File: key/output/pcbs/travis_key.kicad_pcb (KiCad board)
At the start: 2 copper layers, 38.1 x 38.1 mm, 4 parts

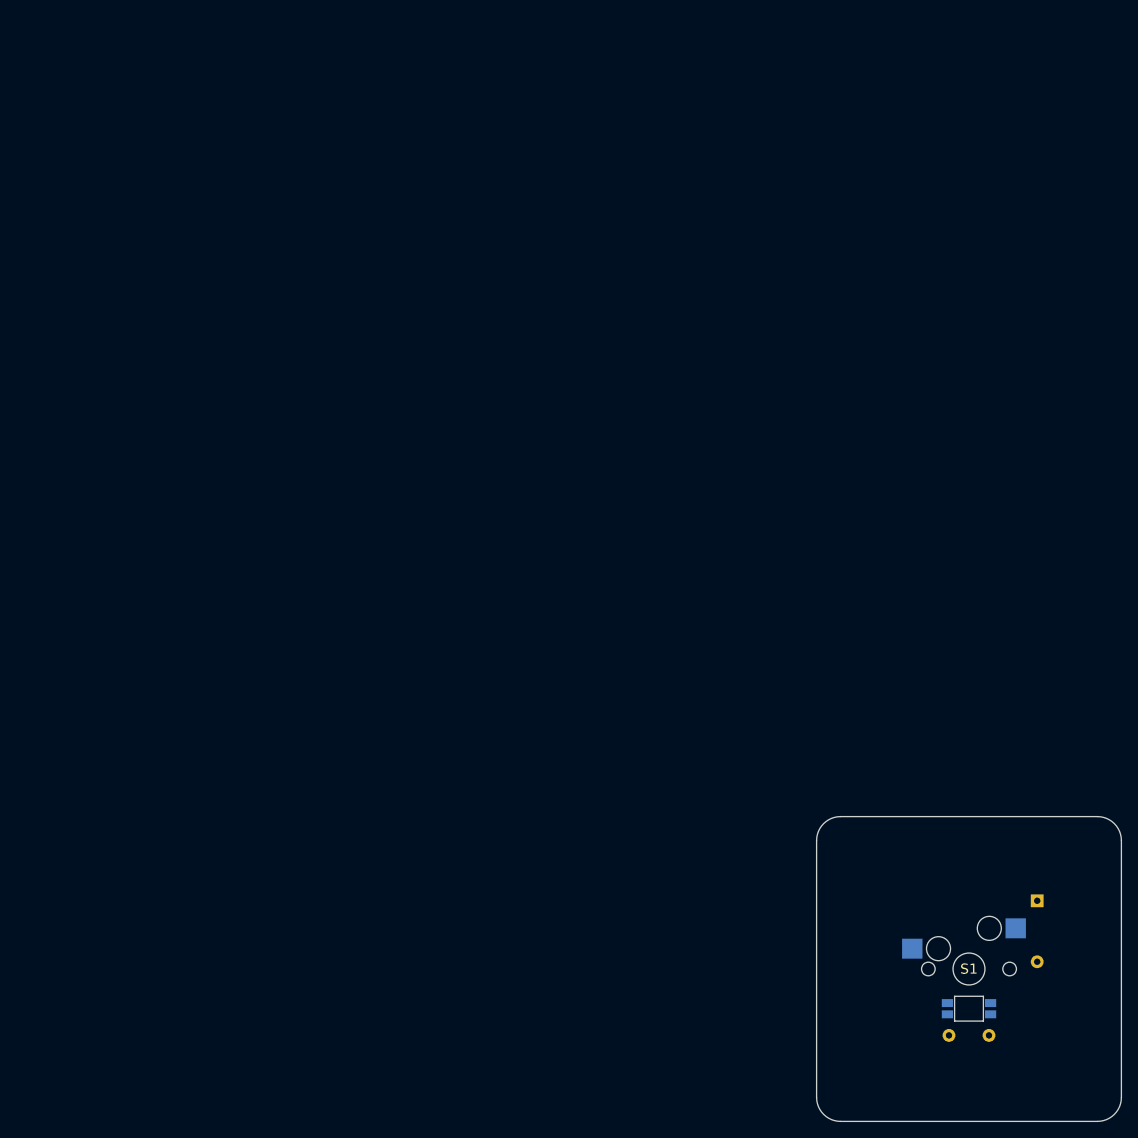
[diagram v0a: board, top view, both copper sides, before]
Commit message: key module functions with traces
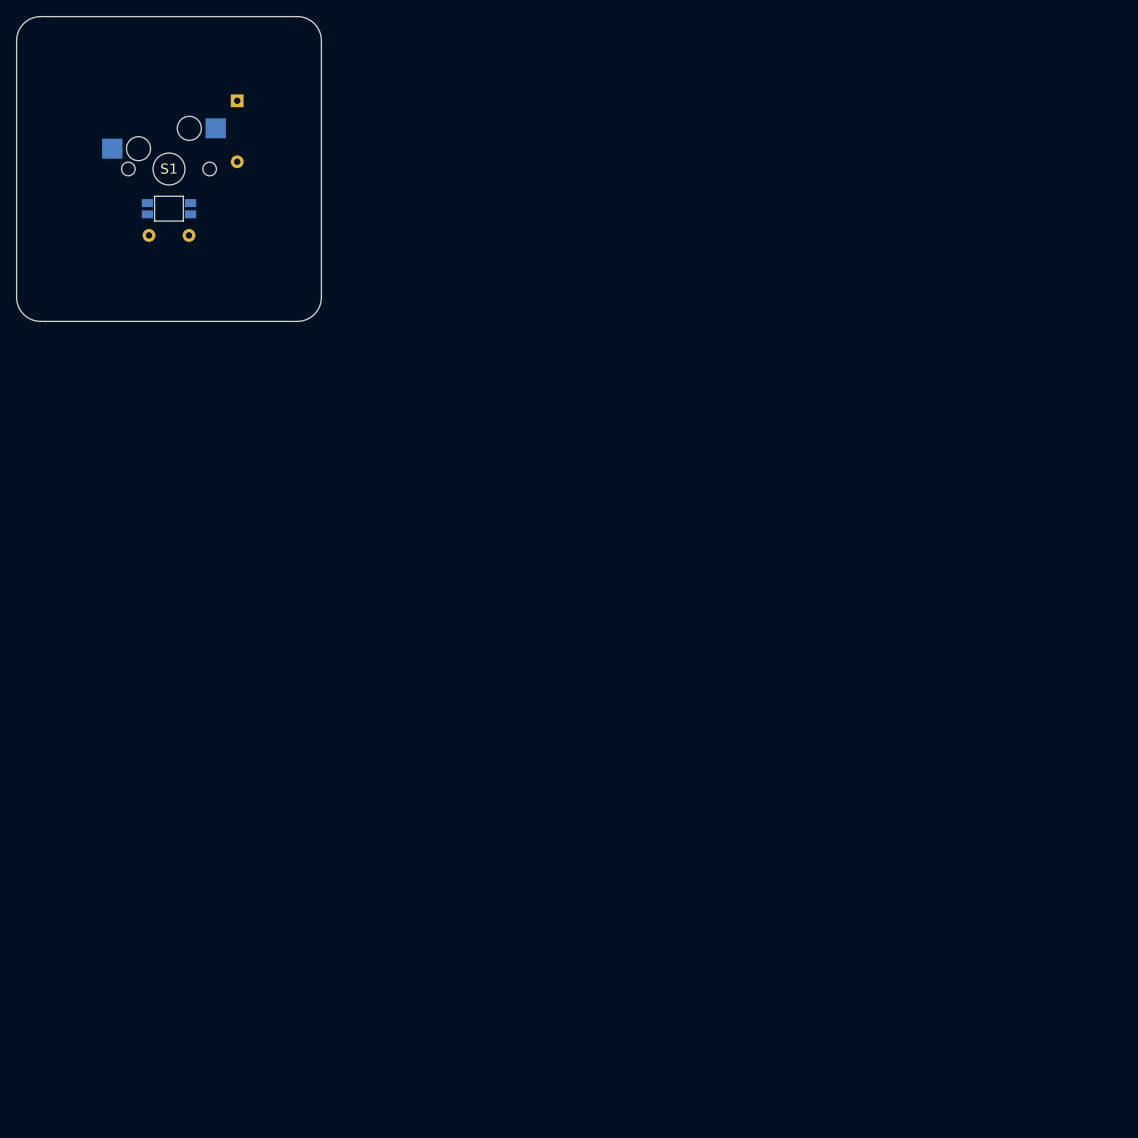
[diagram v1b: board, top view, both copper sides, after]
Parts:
- moved C1 141.4 mm to (2.50, 8.30)
- moved D1 141.4 mm to (8.53, -8.53)
- moved LED1 141.4 mm to (0.00, 4.96)
- moved S1 141.4 mm to (0.00, 0.00)
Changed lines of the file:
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@@
   )
       (module MX (layer F.Cu)
-      (at 100 100 0)
+      (at 0 0 0)
       (fp_text reference "S1" (at 0 0) (layer F.SilkS)  (effects (font (size 1.27 1.27) (thickness 0.15))))
       (fp_text value "" (at 0 0) (layer F.SilkS) hide (effects (font (size 1.27 1.27) (thickness 0.15))))
@@
     (descr "Diode, DO-35_SOD27 series, Axial, Horizontal, pin pitch=7.62mm, , length*diameter=4*2mm^2, , http://www.diodes.com/_files/packages/DO-35.pdf")
     (tags "Diode DO-35_SOD27 series Axial Horizontal pin pitch 7.62mm  length 4mm diameter 2mm")
-    (at 108.525 91.475 270)
+    (at 8.525 -8.525 270)
     (fp_text reference "D1" (at 3.81 -2.12 270) (layer "B.SilkS")
       (effects (font (size 1 1) (thickness 0.15)) (justify mirror))
@@
       (module "ceoloide:led_SK6812mini-e (per-keysingle-side)"
         (layer B.Cu)
-        (at 100 104.96 0)
+        (at 0 4.96 0)
         (fp_text reference "LED1" (at -4.75 0 90) (layer B.SilkS)
           (effects (font (size 1 1) (thickness 0.15)))
@@
         (polygon
           (pts
-            (xy 98.000 103.110)
-            (xy 102.000 103.110)
-            (xy 102.000 106.810)
-            (xy 98.000 106.810)
+            (xy -2.000 3.110)
+            (xy 2.000 3.110)
+            (xy 2.000 6.810)
+            (xy -2.000 6.810)
           )
         )
@@
     (descr "C, Disc series, Radial, pin pitch=5.00mm, , diameter*width=4.7*2.5mm^2, Capacitor, http://www.vishay.com/docs/45233/krseries.pdf")
     (tags "C Disc series Radial pin pitch 5.00mm  diameter 4.7mm width 2.5mm Capacitor")
-    (at 102.5 108.3 180)
+    (at 2.5 8.3 180)
     (fp_text reference "C1" (at 2.5 -2.5 180) (layer B.SilkS)
       (effects (font (size 1 1) (thickness 0.15)) (justify mirror))
     )
     (fp_text value "104" (at 2.5 2.5 180) (layer B.Fab)
-      (effects (font (size 1 1) (thickness 0.15)) (justify mirror))
+      (effects (font (size 1 1) (thickness 0.15)))
     )
     (fp_line (start 0.15 -1.25) (end 0.15 1.25) (layer B.Fab) (width 0.1))
@@
     )
   )
-            (gr_line (start 80.95 116.05) (end 80.95 83.95) (angle 90) (layer Edge.Cuts) (width 0.15))
-(gr_line (start 83.95 80.95) (end 116.05 80.95) (angle 90) (layer Edge.Cuts) (width 0.15))
-(gr_line (start 119.05 83.95) (end 119.05 116.05) (angle 90) (layer Edge.Cuts) (width 0.15))
-(gr_line (start 116.05 119.05) (end 83.95 119.05) (angle 90) (layer Edge.Cuts) (width 0.15))
-(gr_arc (start 83.95 83.95) (end 83.95 80.95) (angle -90) (layer Edge.Cuts) (width 0.15))
-(gr_arc (start 116.05 83.95) (end 119.05 83.95) (angle -90) (layer Edge.Cuts) (width 0.15))
-(gr_arc (start 116.05 116.05) (end 116.05 119.05) (angle -90) (layer Edge.Cuts) (width 0.15))
-(gr_arc (start 83.95 116.05) (end 80.95 116.05) (angle -90) (layer Edge.Cuts) (width 0.15))
+            (gr_line (start -19.05 16.05) (end -19.05 -16.05) (angle 90) (layer Edge.Cuts) (width 0.15))
+(gr_line (start -16.05 -19.05) (end 16.05 -19.05) (angle 90) (layer Edge.Cuts) (width 0.15))
+(gr_line (start 19.05 -16.05) (end 19.05 16.05) (angle 90) (layer Edge.Cuts) (width 0.15))
+(gr_line (start 16.05 19.05) (end -16.05 19.05) (angle 90) (layer Edge.Cuts) (width 0.15))
+(gr_arc (start -16.05 -16.05) (end -16.05 -19.05) (angle -90) (layer Edge.Cuts) (width 0.15))
+(gr_arc (start 16.05 -16.05) (end 19.05 -16.05) (angle -90) (layer Edge.Cuts) (width 0.15))
+(gr_arc (start 16.05 16.05) (end 16.05 19.05) (angle -90) (layer Edge.Cuts) (width 0.15))
+(gr_arc (start -16.05 16.05) (end -19.05 16.05) (angle -90) (layer Edge.Cuts) (width 0.15))
 )

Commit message: footprint wip
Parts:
- LED1: value (none) -> SK6812mini-e; footprint ceoloide:led_SK6812mini-e (per-keysingle-side) -> ceoloide:led_SK6812mini-e (per-key single-side)
- S1: value (none) -> Kailh MX Switch Sockets
- moved D1 0.50 mm to (8.53, -8.03)
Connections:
- net LED_0 renamed LED_2
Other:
- board text added: "C1"
- board text added: "D1"
- board text added: "LED_1"
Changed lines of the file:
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@@
   (title_block
     (title travis_key)
-    (rev 2024.03.20)
+    (rev 2024.03.23)
     (company "Travis Hardiman")
   )
@@
 (net 3 "row0")
 (net 4 "RAW")
-(net 5 "LED_0")
+(net 5 "LED_2")
 (net 6 "GND")
 (net 7 "LED_1")
@@
 (add_net "row0")
 (add_net "RAW")
-(add_net "LED_0")
+(add_net "LED_2")
 (add_net "GND")
 (add_net "LED_1")
   )
-      (module MX (layer F.Cu)
-      (at 0 0 0)
-      (fp_text reference "S1" (at 0 0) (layer F.SilkS)  (effects (font (size 1.27 1.27) (thickness 0.15))))
-      (fp_text value "" (at 0 0) (layer F.SilkS) hide (effects (font (size 1.27 1.27) (thickness 0.15))))
-      (fp_line (start -7 -6) (end -7 -7) (layer Dwgs.User) (width 0.15))
-      (fp_line (start -7 7) (end -6 7) (layer Dwgs.User) (width 0.15))
-      (fp_line (start -6 -7) (end -7 -7) (layer Dwgs.User) (width 0.15))
-      (fp_line (start -7 7) (end -7 6) (layer Dwgs.User) (width 0.15))
-      (fp_line (start 7 6) (end 7 7) (layer Dwgs.User) (width 0.15))
-      (fp_line (start 7 -7) (end 6 -7) (layer Dwgs.User) (width 0.15))
-      (fp_line (start 6 7) (end 7 7) (layer Dwgs.User) (width 0.15))
-      (fp_line (start 7 -7) (end 7 -6) (layer Dwgs.User) (width 0.15))
-      (pad "" np_thru_hole circle (at 0 0) (size 3.9878 3.9878) (drill 3.9878) (layers *.Cu *.Mask))
-      (pad "" np_thru_hole circle (at 5.08 0) (size 1.7018 1.7018) (drill 1.7018) (layers *.Cu *.Mask))
-      (pad "" np_thru_hole circle (at -5.08 0) (size 1.7018 1.7018) (drill 1.7018) (layers *.Cu *.Mask))
-      (fp_line (start -9.5 -9.5) (end 9.5 -9.5) (layer Dwgs.User) (width 0.15))
-      (fp_line (start 9.5 -9.5) (end 9.5 9.5) (layer Dwgs.User) (width 0.15))
-      (fp_line (start 9.5 9.5) (end -9.5 9.5) (layer Dwgs.User) (width 0.15))
-      (fp_line (start -9.5 9.5) (end -9.5 -9.5) (layer Dwgs.User) (width 0.15))
-        (pad "" np_thru_hole circle (at 2.54 -5.08) (size 3 3) (drill 3) (layers *.Cu *.Mask))
-        (pad "" np_thru_hole circle (at -3.81 -2.54) (size 3 3) (drill 3) (layers *.Cu *.Mask))
-        (pad 1 smd rect (at -7.085 -2.54 0) (size 2.55 2.5) (layers B.Cu B.Paste B.Mask) (net 1 "col0"))
-        (pad 2 smd rect (at 5.842 -5.08 0) (size 2.55 2.5) (layers B.Cu B.Paste B.Mask) (net 2 "single_A_one"))
-        )
+        (module MX (layer F.Cu)
+        (at 0 0 0)
+        (fp_text reference "S1" (at 0 -3.25) (layer F.SilkS)  (effects (font (size 1 1) (thickness 0.15))))
+        (fp_text value "Kailh MX Switch Sockets" (at 0 0) (layer B.Fab) hide (effects (font (size 1 1) (thickness 0.15))))
+        (fp_line (start -7 -6) (end -7 -7) (layer Dwgs.User) (width 0.15))
+        (fp_line (start -7 7) (end -6 7) (layer Dwgs.User) (width 0.15))
+        (fp_line (start -6 -7) (end -7 -7) (layer Dwgs.User) (width 0.15))
+        (fp_line (start -7 7) (end -7 6) (layer Dwgs.User) (width 0.15))
+        (fp_line (start 7 6) (end 7 7) (layer Dwgs.User) (width 0.15))
+        (fp_line (start 7 -7) (end 6 -7) (layer Dwgs.User) (width 0.15))
+        (fp_line (start 6 7) (end 7 7) (layer Dwgs.User) (width 0.15))
+        (fp_line (start 7 -7) (end 7 -6) (layer Dwgs.User) (width 0.15))
+        (pad "" np_thru_hole circle (at 0 0) (size 3.9878 3.9878) (drill 3.9878) (layers *.Cu *.Mask))
+        (pad "" np_thru_hole circle (at 5.08 0) (size 1.7018 1.7018) (drill 1.7018) (layers *.Cu *.Mask))
+        (pad "" np_thru_hole circle (at -5.08 0) (size 1.7018 1.7018) (drill 1.7018) (layers *.Cu *.Mask))
+        (fp_line (start -9.5 -9.5) (end 9.5 -9.5) (layer Dwgs.User) (width 0.15))
+        (fp_line (start 9.5 -9.5) (end 9.5 9.5) (layer Dwgs.User) (width 0.15))
+        (fp_line (start 9.5 9.5) (end -9.5 9.5) (layer Dwgs.User) (width 0.15))
+        (fp_line (start -9.5 9.5) (end -9.5 -9.5) (layer Dwgs.User) (width 0.15))
+          (pad "" np_thru_hole circle (at 2.54 -5.08) (size 3 3) (drill 3) (layers *.Cu *.Mask))
+          (pad "" np_thru_hole circle (at -3.81 -2.54) (size 3 3) (drill 3) (layers *.Cu *.Mask))
+          (pad 1 smd rect (at -7.085 -2.54 0) (size 2.55 2.5) (layers B.Cu B.Paste B.Mask) (net 1 "col0"))
+          (pad 2 smd rect (at 5.842 -5.08 0) (size 2.55 2.5) (layers B.Cu B.Paste B.Mask) (net 2 "single_A_one"))
+      (model "${SCOTTOKEEBS_KICAD}/3dmodels/ScottoKeebs_Hotswap.3dshapes/Hotswap_MX.step"
+		(offset (xyz 0 0 0) )
+		(scale (xyz 1 1 1) )
+		(rotate (xyz 0 0 0) )
+	  ))
     (module "Diode_DO-35" (layer "B.Cu")
     (descr "Diode, DO-35_SOD27 series, Axial, Horizontal, pin pitch=7.62mm, , length*diameter=4*2mm^2, , http://www.diodes.com/_files/packages/DO-35.pdf")
     (tags "Diode DO-35_SOD27 series Axial Horizontal pin pitch 7.62mm  length 4mm diameter 2mm")
-    (at 8.525 -8.525 270)
-    (fp_text reference "D1" (at 3.81 -2.12 270) (layer "B.SilkS")
+    (at 8.525 -8.025 270)
+    (fp_text reference "D1" (at 5.985 1.921 270) (layer "B.SilkS")
       (effects (font (size 1 1) (thickness 0.15)) (justify mirror))
     )
-    (fp_text value "1N4148" (at 3.81 0 270) (layer "B.Fab")
-      (effects (font (size 0.8 1) (thickness 0.15)))
-    )
-    (fp_text user "K" (at 0 -1.8 270) (layer "B.SilkS")
-      (effects (font (size 1 1) (thickness 0.15)) (justify mirror))
-    )
-    (fp_text user "K" (at 0 -1.8 270) (layer "B.Fab")
-      (effects (font (size 1 1) (thickness 0.15)) (justify mirror))
+    (fp_text value "1N4148" (at 11.065 0 270) (layer "B.Fab")
+      (effects (font (size 0.8 0.8) (thickness 0.15)))
     )
     (fp_line (start 1.04 0) (end 1.69 0)
@@
     )
   )
-      (module "ceoloide:led_SK6812mini-e (per-keysingle-side)"
+      (gr_text "D1" (at 7.525 -4.215 0) (layer F.SilkS)
+        (effects (font (size 0.9 0.9) (thickness 0.15)) (justify left))
+      )
+      (module "ceoloide:led_SK6812mini-e (per-key single-side)"
         (layer B.Cu)
         (at 0 4.96 0)
-        (fp_text reference "LED1" (at -4.75 0 90) (layer B.SilkS)
-          (effects (font (size 1 1) (thickness 0.15)))
+        (fp_text reference "LED1" (at -5.25 0 90) (layer B.SilkS)
+          (effects (font (size 1 1) (thickness 0.15)) (justify  mirror))
+        )
+        (fp_text value "SK6812mini-e" (at 0 -2.25 0) (layer "B.Fab")
+          (effects (font (size 0.8 0.8) (thickness 0.15)))
         )
         (fp_line (start -1.6 -1.4) (end 1.6 -1.4) (layer Dwgs.User) (width 0.12))
@@
         (fp_line (start -3.8 -1.6) (end -2.2 -1.6) (layer B.SilkS) (width 0.12))
         (fp_line (start -3.8 0) (end -3.8 -1.6) (layer B.SilkS) (width 0.12))
-        (pad 2 smd rect (at 2.70 -0.7 0) (size 1.4 1) (layers B.Cu B.Paste B.Mask) (net 5 "LED_0"))
+        (fp_line (start -3.8 -1.36) (end -3.56 -1.6) (layer B.SilkS) (width 0.12))
+        (pad 2 smd rect (at 2.70 -0.7 0) (size 1.4 1) (layers B.Cu B.Paste B.Mask) (net 5 "LED_2"))
         (pad 1 smd rect (at 2.70 0.7 0) (size 1.4 1) (layers B.Cu B.Paste B.Mask) (net 4 "RAW"))
         (pad 3 smd rect (at -2.70 -0.7 0) (size 1.4 1) (layers B.Cu B.Paste B.Mask) (net 6 "GND"))
@@
         )
       )
+      (gr_text "LED_1" (at -2.7 5.66 0) (layer F.SilkS)
+        (effects (font (size 0.8 0.8) (thickness 0.15)) (justify right))
+      )
     (module C_Disc_D4.7mm_W2.5mm_P5.00mm (layer B.Cu)
     (descr "C, Disc series, Radial, pin pitch=5.00mm, , diameter*width=4.7*2.5mm^2, Capacitor, http://www.vishay.com/docs/45233/krseries.pdf")
     (tags "C Disc series Radial pin pitch 5.00mm  diameter 4.7mm width 2.5mm Capacitor")
     (at 2.5 8.3 180)
-    (fp_text reference "C1" (at 2.5 -2.5 180) (layer B.SilkS)
+    (fp_text reference "C1" (at 7.5 0 180) (layer B.SilkS)
       (effects (font (size 1 1) (thickness 0.15)) (justify mirror))
     )
-    (fp_text value "104" (at 2.5 2.5 180) (layer B.Fab)
+    (fp_text value "104" (at -2.5 0 180) (layer B.Fab)
       (effects (font (size 1 1) (thickness 0.15)))
     )
@@
     (pad 1 thru_hole circle (at 0 0) (size 1.6 1.6) (drill 0.8) (layers *.Cu *.Mask) (net 4 "RAW"))
     (pad 2 thru_hole circle (at 5 0) (size 1.6 1.6) (drill 0.8) (layers *.Cu *.Mask) (net 6 "GND"))
-    (fp_text user %R (at 2.5 0) (layer B.Fab)
-      (effects (font (size 0.94 0.94) (thickness 0.141)))
-    )
     (model ${KISYS3DMOD}/Capacitor_THT.3dshapes/C_Disc_D4.7mm_W2.5mm_P5.00mm.wrl
       (at (xyz 0 0 0))
@@
     )
   )
+      (gr_text "C1" (at 0 8.3 0) (layer F.SilkS)
+        (effects (font (size 0.9 0.9) (thickness 0.15)))
+      )
             (gr_line (start -19.05 16.05) (end -19.05 -16.05) (angle 90) (layer Edge.Cuts) (width 0.15))
 (gr_line (start -16.05 -19.05) (end 16.05 -19.05) (angle 90) (layer Edge.Cuts) (width 0.15))
